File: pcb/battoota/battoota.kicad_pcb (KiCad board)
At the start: 2 copper layers, 128.3 x 99.3 mm, 38 parts

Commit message: fix gnd  issue in 30 keys
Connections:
- MCU1 pad 16: GND -> (no net)
- MCU1 pad 2: Bgnd -> GND
- PAD1 pad 2: Bgnd -> GND
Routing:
- net GND: track 254.5 -> 304.7 mm, vias 0 -> 1
- net Bgnd: track 50.2 -> 0.00 mm, vias 1 -> 0
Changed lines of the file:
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@@
   (net 20 "VCC")
   (net 21 "Braw")
-  (net 22 "Bgnd")
   (footprint "E73:SPDT_C128955" (layer "F.Cu")
     (at 162.242148 -55.849495 -90)
@@
       (net 21 "Braw"))
     (pad "2" thru_hole roundrect locked (at 0 0) (size 1.5 2.25) (drill 1.0922) (layers *.Cu *.SilkS *.Mask) (roundrect_rratio 0.25)
-      (net 22 "Bgnd"))
+      (net 2 "GND"))
     (pad "3" thru_hole roundrect locked (at -2 0) (size 1.5 2.25) (drill 1.0922) (layers *.Cu *.SilkS *.Mask) (roundrect_rratio 0.25)
       (net 21 "Braw"))
@@
       ))
     (pad "2" smd custom (at -11.43 3.913523 180) (size 0.3 0.3) (layers "F.Cu" "F.Mask")
-      (net 22 "Bgnd") (zone_connect 2)
+      (net 2 "GND") (zone_connect 2)
       (options (clearance outline) (anchor rect))
       (primitives
@@
       ))
     (pad "2" smd custom (at -11.43 -3.836477 180) (size 0.3 0.3) (layers "B.Cu" "B.Mask")
-      (net 22 "Bgnd") (zone_connect 2)
+      (net 2 "GND") (zone_connect 2)
       (options (clearance outline) (anchor rect))
       (primitives
@@
     (pad "12" thru_hole circle (at 13.97 7.62) (size 1.7526 1.7526) (drill 1.0922) (layers *.Cu *.SilkS *.Mask)
       (net 11 "P10"))
-    (pad "16" thru_hole circle (at -6.35 -7.62) (size 1.7526 1.7526) (drill 1.0922) (layers *.Cu *.SilkS *.Mask)
-      (net 2 "GND"))
+    (pad "16" thru_hole circle (at -6.35 -7.62) (size 1.7526 1.7526) (drill 1.0922) (layers *.Cu *.SilkS *.Mask))
     (pad "17" thru_hole circle (at -3.81 -7.62) (size 1.7526 1.7526) (drill 1.0922) (layers *.Cu *.SilkS *.Mask)
       (net 6 "P2"))
@@
   (segment (start 127.939105 -43.339776) (end 125.807135 -45.471746) (width 0.5) (layer "F.Cu") (net 2))
   (segment (start 148.041805 -36.250663) (end 144.4244 -39.868068) (width 0.5) (layer "F.Cu") (net 2))
+  (segment (start 154.256703 -98.602542) (end 150.44369 -98.602542) (width 0.5) (layer "F.Cu") (net 2))
   (segment (start 108.15356 -76.015027) (end 107.136087 -77.0325) (width 0.5) (layer "F.Cu") (net 2))
   (segment (start 109.566271 -100.786017) (end 107.136087 -103.216201) (width 0.5) (layer "F.Cu") (net 2))
@@
   (segment (start 88.013843 -91.236618) (end 85.651298 -93.599163) (width 0.5) (layer "F.Cu") (net 2))
   (segment (start 108.973745 -83.786017) (end 107.136087 -85.623675) (width 0.5) (layer "F.Cu") (net 2))
+  (segment (start 154.304587 -98.650426) (end 154.256703 -98.602542) (width 0.5) (layer "F.Cu") (net 2))
   (segment (start 128.150955 -90.410985) (end 126.242334 -92.319606) (width 0.5) (layer "F.Cu") (net 2))
   (segment (start 44.864298 -78.586881) (end 44.864298 -82.864875) (width 0.5) (layer "F.Cu") (net 2))
@@
   (segment (start 126.242334 -75.958503) (end 126.242334 -83.060985) (width 0.5) (layer "F.Cu") (net 2))
   (segment (start 84.169651 -110.541422) (end 84.169651 -117.063993) (width 0.5) (layer "F.Cu") (net 2))
+  (via (at 154.304587 -98.650426) (size 0.8) (drill 0.4) (layers "F.Cu" "B.Cu") (free) (net 2))
+  (segment (start 154.329345 -98.675184) (end 154.329345 -64.825511) (width 0.5) (layer "B.Cu") (net 2))
+  (segment (start 149.545396 -60.041562) (end 149.545396 -58.163682) (width 0.5) (layer "B.Cu") (net 2))
+  (segment (start 154.329345 -64.825511) (end 149.545396 -60.041562) (width 0.5) (layer "B.Cu") (net 2))
+  (segment (start 154.304587 -98.650426) (end 154.329345 -98.675184) (width 0.5) (layer "B.Cu") (net 2))
+  (segment (start 154.329345 -98.675184) (end 158.139502 -98.675184) (width 0.5) (layer "B.Cu") (net 2))
   (segment (start 154.178854 -72.532303) (end 154.178854 -80.140845) (width 0.25) (layer "F.Cu") (net 3))
   (segment (start 157.383378 -83.345369) (end 161.96004 -83.345369) (width 0.25) (layer "F.Cu") (net 3))
@@
   (segment (start 151.609583 -58.099495) (end 151.545396 -58.163682) (width 0.5) (layer "B.Cu") (net 21))
   (segment (start 160.167148 -58.099495) (end 151.609583 -58.099495) (width 0.5) (layer "B.Cu") (net 21))
-  (segment (start 154.256703 -98.602542) (end 150.44369 -98.602542) (width 0.5) (layer "F.Cu") (net 22))
-  (segment (start 154.304587 -98.650426) (end 154.256703 -98.602542) (width 0.5) (layer "F.Cu") (net 22))
-  (via (at 154.304587 -98.650426) (size 0.8) (drill 0.4) (layers "F.Cu" "B.Cu") (free) (net 22))
-  (segment (start 154.329345 -98.675184) (end 154.329345 -64.825511) (width 0.5) (layer "B.Cu") (net 22))
-  (segment (start 149.545396 -60.041562) (end 149.545396 -58.163682) (width 0.5) (layer "B.Cu") (net 22))
-  (segment (start 154.329345 -64.825511) (end 149.545396 -60.041562) (width 0.5) (layer "B.Cu") (net 22))
-  (segment (start 154.304587 -98.650426) (end 154.329345 -98.675184) (width 0.5) (layer "B.Cu") (net 22))
-  (segment (start 154.329345 -98.675184) (end 158.139502 -98.675184) (width 0.5) (layer "B.Cu") (net 22))
   (zone (net 2) (net_name "GND") (layer "B.Cu") (hatch edge 0.508)
     (connect_pads (clearance 0.508))

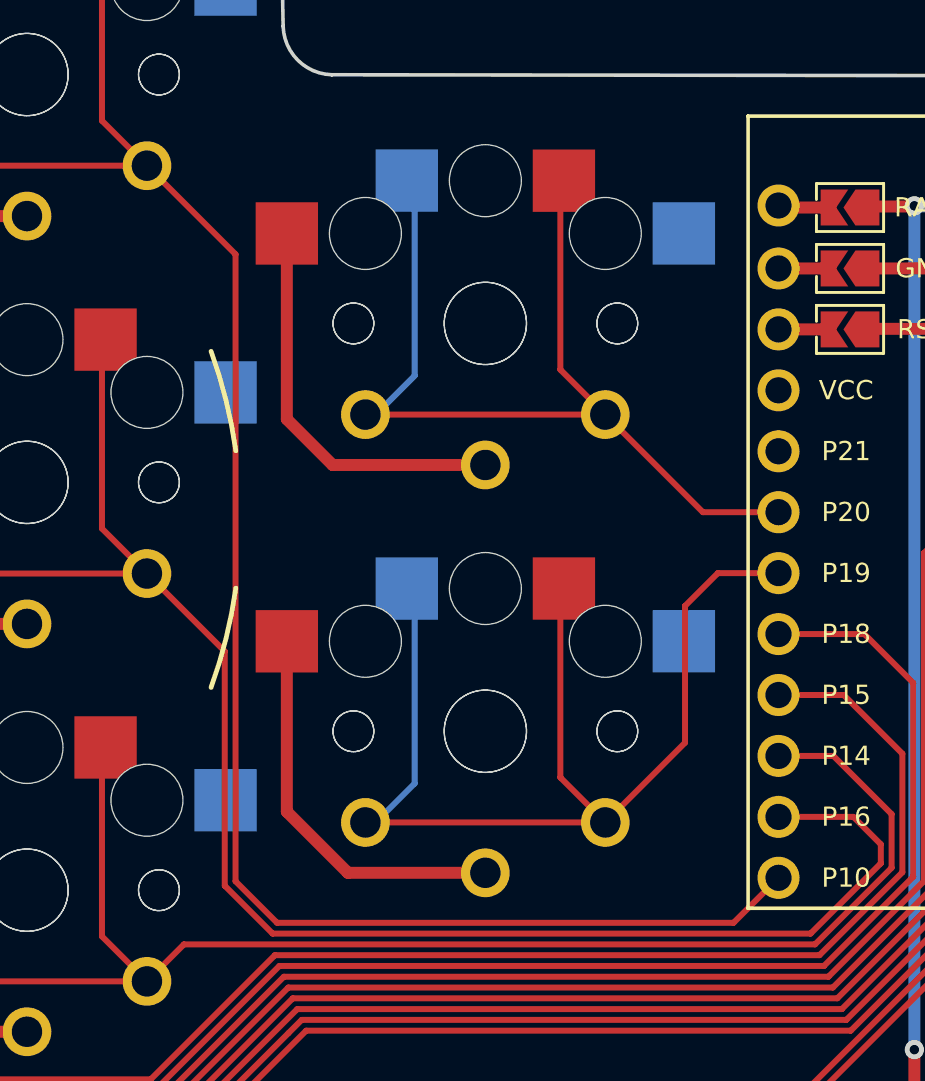
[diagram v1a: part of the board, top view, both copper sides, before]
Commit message: remove curvy and make inner index closer
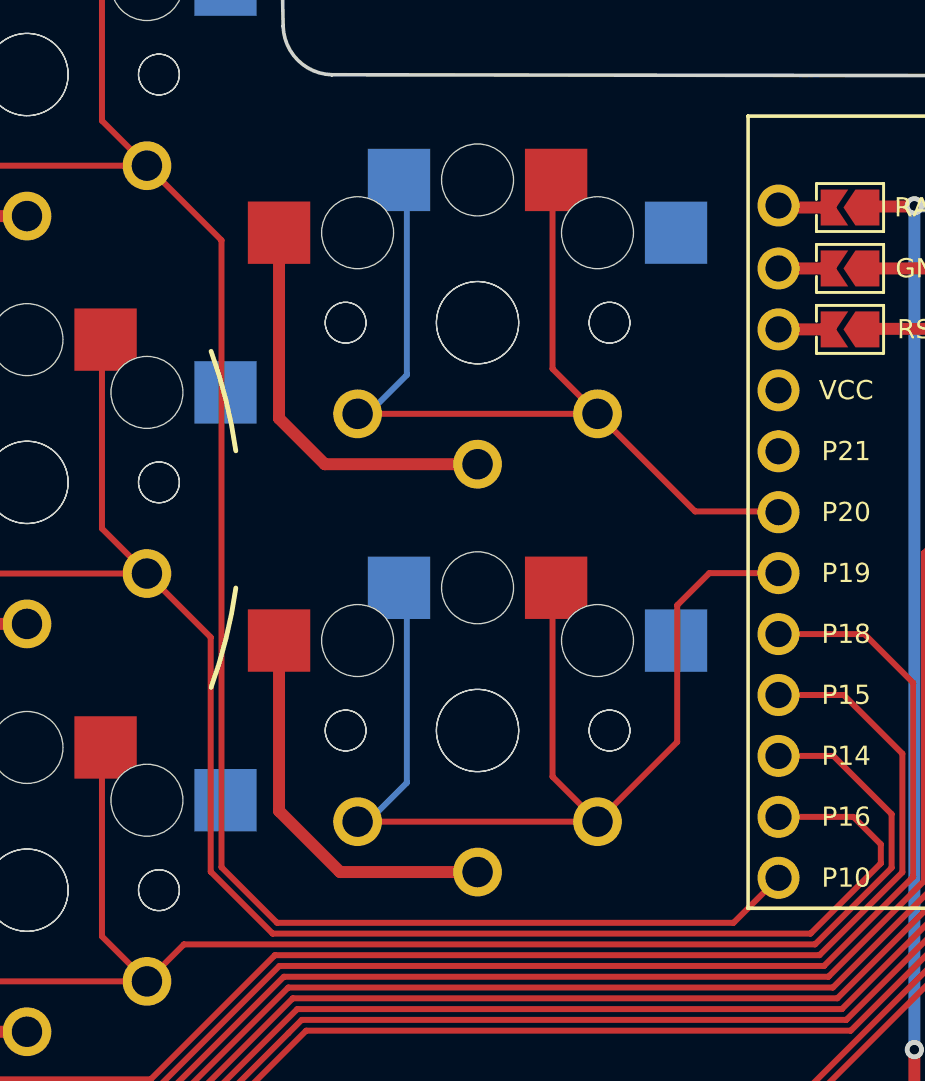
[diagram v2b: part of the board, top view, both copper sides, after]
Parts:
- moved S27 0.33 mm to (134.2, -79.3)
- moved S28 0.33 mm to (134.2, -79.3)
- moved S29 0.33 mm to (134.2, -96.3)
- moved S30 0.33 mm to (134.2, -96.3)

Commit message: update battoota design
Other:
- board size 128.3 x 99.3 mm -> 124.7 x 97.3 mm
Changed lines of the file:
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@@
       ) (layer "B.SilkS") (width 0) (fill solid))
   )
-  (gr_arc (start 104.509588 -117.005368) (mid 103.158397 -117.530806) (end 102.517198 -118.831058) (layer "Edge.Cuts") (width 0.15))
-  (gr_line (start 126.088253 -108.703396) (end 125.984 -114.046) (layer "Edge.Cuts") (width 0.15))
-  (gr_arc (start 82.233091 -118.259454) (mid 81.827408 -116.867619) (end 80.587997 -116.115527) (layer "Edge.Cuts") (width 0.15))
-  (gr_arc (start 167.528587 -47.330455) (mid 168.024672 -45.267049) (end 167.64 -43.18) (layer "Edge.Cuts") (width 0.15))
-  (gr_arc (start 167.528587 -47.330455) (mid 165.211835 -51.649611) (end 164.411087 -56.485027) (layer "Edge.Cuts") (width 0.15))
-  (gr_line (start 60.120825 -110.475759) (end 61.630489 -101.874615) (layer "Edge.Cuts") (width 0.15))
-  (gr_line (start 118.067797 -41.80264) (end 52.13573 -54.028933) (layer "Edge.Cuts") (width 0.15))
-  (gr_line (start 83.834124 -122.906984) (end 99.972478 -124.318907) (layer "Edge.Cuts") (width 0.15))
-  (gr_arc (start 52.13573 -54.028933) (mid 51.093996 -54.760565) (end 50.45086 -55.859129) (layer "Edge.Cuts") (width 0.15))
-  (gr_line (start 162.411086 -106.629429) (end 128.117202 -106.676472) (layer "Edge.Cuts") (width 0.15))
-  (gr_line (start 104.509588 -117.005368) (end 123.444 -116.84) (layer "Edge.Cuts") (width 0.15))
-  (gr_line (start 39.815446 -88.161643) (end 50.45086 -55.859129) (layer "Edge.Cuts") (width 0.15))
-  (gr_arc (start 99.972478 -124.318908) (mid 101.432366 -123.858608) (end 102.139179 -122.500829) (layer "Edge.Cuts") (width 0.15))
-  (gr_arc (start 128.117202 -106.676472) (mid 126.698658 -107.285463) (end 126.088253 -108.703396) (layer "Edge.Cuts") (width 0.15))
-  (gr_arc (start 60.120826 -110.475759) (mid 60.452137 -111.970208) (end 61.743144 -112.792671) (layer "Edge.Cuts") (width 0.15))
-  (gr_line (start 156.354214 -25.985787) (end 167.64 -43.18) (layer "Edge.Cuts") (width 0.15))
-  (gr_arc (start 118.067797 -41.80264) (mid 120.992158 -41.190657) (end 123.746692 -40.034594) (layer "Edge.Cuts") (width 0.15))
-  (gr_line (start 152.4 -25.4) (end 123.746692 -40.034594) (layer "Edge.Cuts") (width 0.15))
-  (gr_arc (start 123.444 -116.84) (mid 125.278785 -115.956422) (end 125.984 -114.046) (layer "Edge.Cuts") (width 0.15))
-  (gr_arc (start 156.354214 -25.985787) (mid 154.473897 -25.039536) (end 152.4 -25.4) (layer "Edge.Cuts") (width 0.15))
-  (gr_arc (start 39.815446 -88.161643) (mid 39.788585 -89.36909) (end 40.458272 -90.379598) (layer "Edge.Cuts") (width 0.15))
-  (gr_line (start 102.139179 -122.500829) (end 102.517198 -118.831058) (layer "Edge.Cuts") (width 0.15))
-  (gr_line (start 61.743144 -112.792671) (end 80.587997 -116.115527) (layer "Edge.Cuts") (width 0.15))
-  (gr_arc (start 61.630489 -101.874615) (mid 61.532287 -100.734816) (end 60.891088 -99.781795) (layer "Edge.Cuts") (width 0.15))
-  (gr_arc (start 82.016046 -120.740284) (mid 82.476347 -122.20017) (end 83.834124 -122.906984) (layer "Edge.Cuts") (width 0.15))
-  (gr_line (start 40.458272 -90.379598) (end 60.891088 -99.781795) (layer "Edge.Cuts") (width 0.15))
-  (gr_line (start 82.23309 -118.259454) (end 82.016046 -120.740283) (layer "Edge.Cuts") (width 0.15))
-  (gr_arc (start 162.411086 -106.629429) (mid 163.838502 -106.070136) (end 164.411086 -104.648) (layer "Edge.Cuts") (width 0.15))
-  (gr_line (start 164.411087 -56.485027) (end 164.411086 -104.648) (layer "Edge.Cuts") (width 0.15))
+  (gr_line (start 126.121408 -108.433191) (end 126.017155 -113.775795) (layer "Edge.Cuts") (width 0.15))
+  (gr_arc (start 123.477155 -116.569795) (mid 125.311947 -115.686235) (end 126.017155 -113.775795) (layer "Edge.Cuts") (width 0.15))
+  (gr_arc (start 39.848601 -87.891438) (mid 39.8224 -89.101164) (end 40.491427 -90.109393) (layer "Edge.Cuts") (width 0.15))
+  (gr_line (start 153.591046 -26.958397) (end 123.779847 -39.764389) (layer "Edge.Cuts") (width 0.15))
+  (gr_arc (start 128.150357 -106.406267) (mid 126.731785 -107.015227) (end 126.121408 -108.433191) (layer "Edge.Cuts") (width 0.15))
+  (gr_line (start 102.172334 -122.230624) (end 102.550353 -118.560853) (layer "Edge.Cuts") (width 0.15))
+  (gr_line (start 82.266245 -117.989249) (end 82.049201 -120.470078) (layer "Edge.Cuts") (width 0.15))
+  (gr_arc (start 60.153981 -110.205554) (mid 60.48529 -111.700005) (end 61.776299 -112.522466) (layer "Edge.Cuts") (width 0.15))
+  (gr_arc (start 52.168885 -53.758728) (mid 51.127162 -54.490363) (end 50.484015 -55.588924) (layer "Edge.Cuts") (width 0.15))
+  (gr_arc (start 82.266246 -117.989249) (mid 81.860585 -116.597398) (end 80.621152 -115.845322) (layer "Edge.Cuts") (width 0.15))
+  (gr_arc (start 162.444241 -106.359224) (mid 163.871637 -105.799912) (end 164.444241 -104.377795) (layer "Edge.Cuts") (width 0.15))
+  (gr_line (start 162.444241 -106.359224) (end 128.150357 -106.406267) (layer "Edge.Cuts") (width 0.15))
+  (gr_line (start 40.491427 -90.109393) (end 60.924243 -99.51159) (layer "Edge.Cuts") (width 0.15))
+  (gr_line (start 61.776299 -112.522466) (end 80.621152 -115.845322) (layer "Edge.Cuts") (width 0.15))
+  (gr_line (start 118.100952 -41.532435) (end 52.168885 -53.758728) (layer "Edge.Cuts") (width 0.15))
+  (gr_line (start 157.367946 -28.458049) (end 163.435813 -39.438858) (layer "Edge.Cuts") (width 0.15))
+  (gr_arc (start 82.049201 -120.470079) (mid 82.509504 -121.929964) (end 83.867279 -122.636779) (layer "Edge.Cuts") (width 0.15))
+  (gr_arc (start 118.100952 -41.532435) (mid 121.025117 -40.920519) (end 123.779847 -39.764389) (layer "Edge.Cuts") (width 0.15))
+  (gr_line (start 39.848601 -87.891438) (end 50.484015 -55.588924) (layer "Edge.Cuts") (width 0.15))
+  (gr_arc (start 157.367946 -28.458049) (mid 155.764262 -26.991042) (end 153.591046 -26.958397) (layer "Edge.Cuts") (width 0.15))
+  (gr_line (start 60.15398 -110.205554) (end 61.663644 -101.60441) (layer "Edge.Cuts") (width 0.15))
+  (gr_line (start 104.542743 -116.735163) (end 123.477155 -116.569795) (layer "Edge.Cuts") (width 0.15))
+  (gr_arc (start 100.005633 -124.048703) (mid 101.465554 -123.588422) (end 102.172334 -122.230624) (layer "Edge.Cuts") (width 0.15))
+  (gr_arc (start 61.663644 -101.60441) (mid 61.564659 -100.462355) (end 60.924243 -99.51159) (layer "Edge.Cuts") (width 0.15))
+  (gr_arc (start 104.542743 -116.735163) (mid 103.191579 -117.260624) (end 102.550353 -118.560853) (layer "Edge.Cuts") (width 0.15))
+  (gr_line (start 83.867279 -122.636779) (end 100.005633 -124.048702) (layer "Edge.Cuts") (width 0.15))
+  (gr_line (start 164.473079 -43.609992) (end 164.444241 -104.377795) (layer "Edge.Cuts") (width 0.15))
+  (gr_arc (start 164.473079 -43.609992) (mid 164.184386 -41.467243) (end 163.435813 -39.438858) (layer "Edge.Cuts") (width 0.15))
   (segment (start 157.527339 -80.822542) (end 154.628374 -77.923577) (width 0.25) (layer "F.Cu") (net 1))
   (segment (start 58.734795 -80.557863) (end 52.095465 -80.557863) (width 0.25) (layer "F.Cu") (net 1))

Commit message: pcb shape change
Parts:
- moved B1 0.53 mm to (163.1, -66.1)
- moved T1 0.35 mm to (162.6, -55.7)
- moved T2 0.35 mm to (162.6, -55.7)
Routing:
- net Braw: track 35.8 -> 37.1 mm
- net RST: track 38.3 -> 38.8 mm
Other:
- board size 124.7 x 97.3 mm -> 125.1 x 97.3 mm
